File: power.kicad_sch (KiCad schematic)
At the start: 14 parts, among them J3 RAPC722X, J4 Screw_Terminal_01x02, J5 5V, J6 GND, U3 LM2576HVS-5, U4 LM2576HVS-5

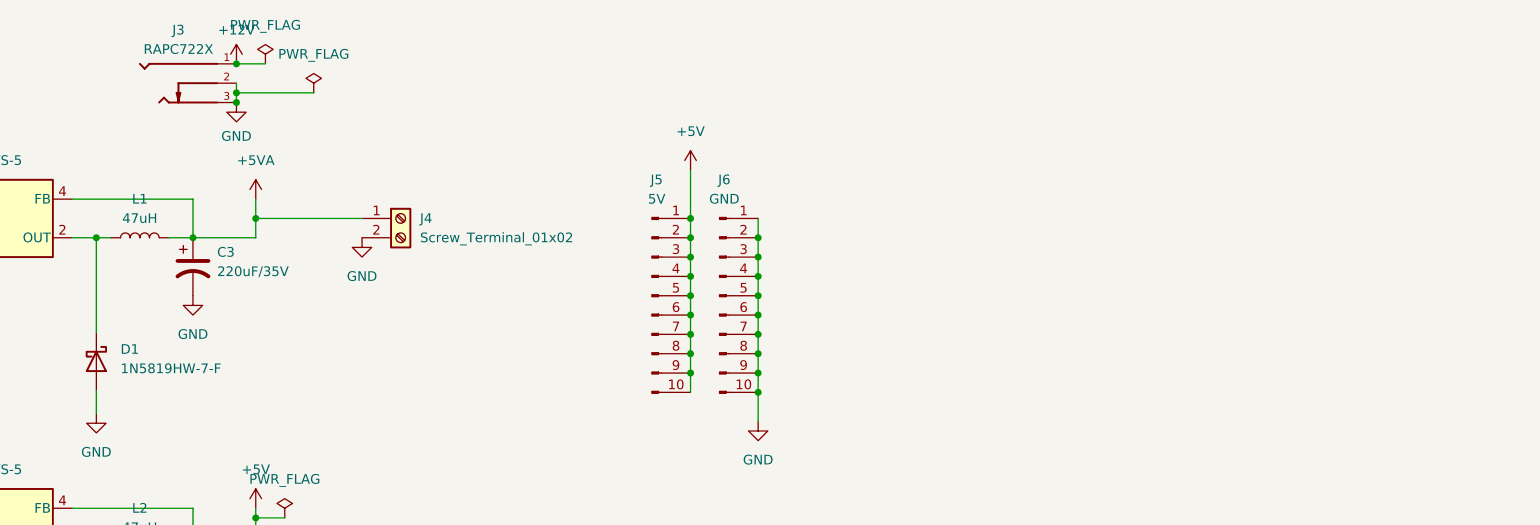
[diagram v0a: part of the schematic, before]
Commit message: Added motor driver
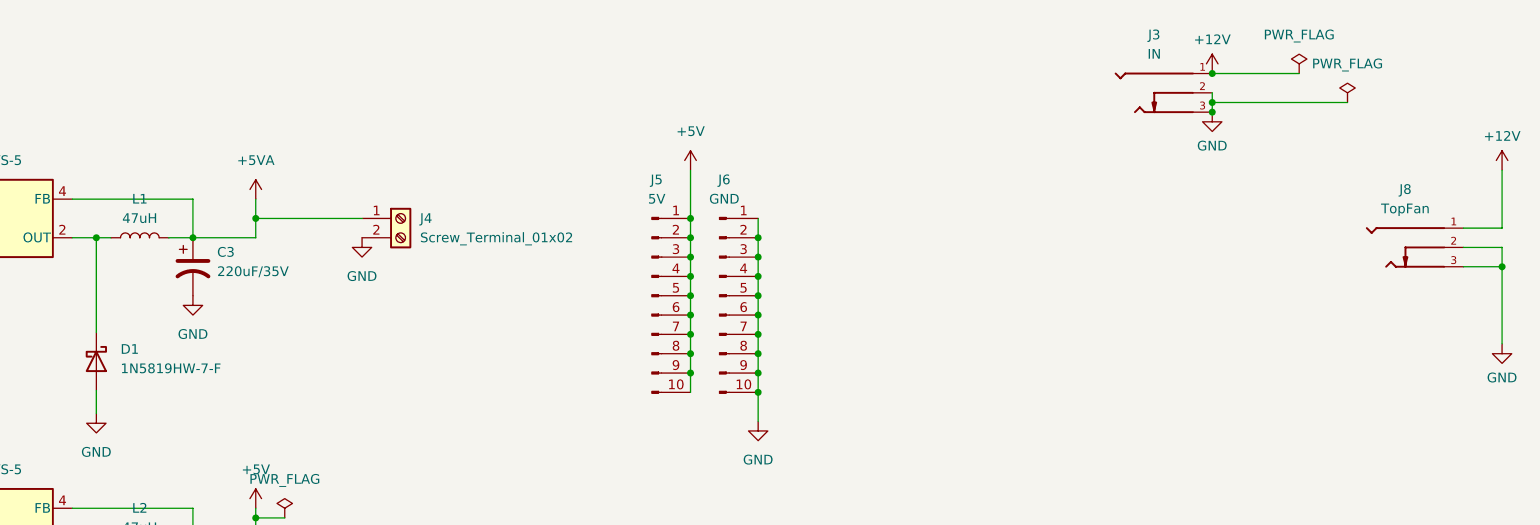
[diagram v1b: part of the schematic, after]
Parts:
- added J8: TopFan, Downloaded_footprints:SWITCHCRAFT_RAPC722X, symbol RAPC722X:RAPC722X
- J3: value RAPC722X -> IN
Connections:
- net +12V: now also J8.1
- net GND: now also J8.2, J8.3
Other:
- moved on the sheet: J3

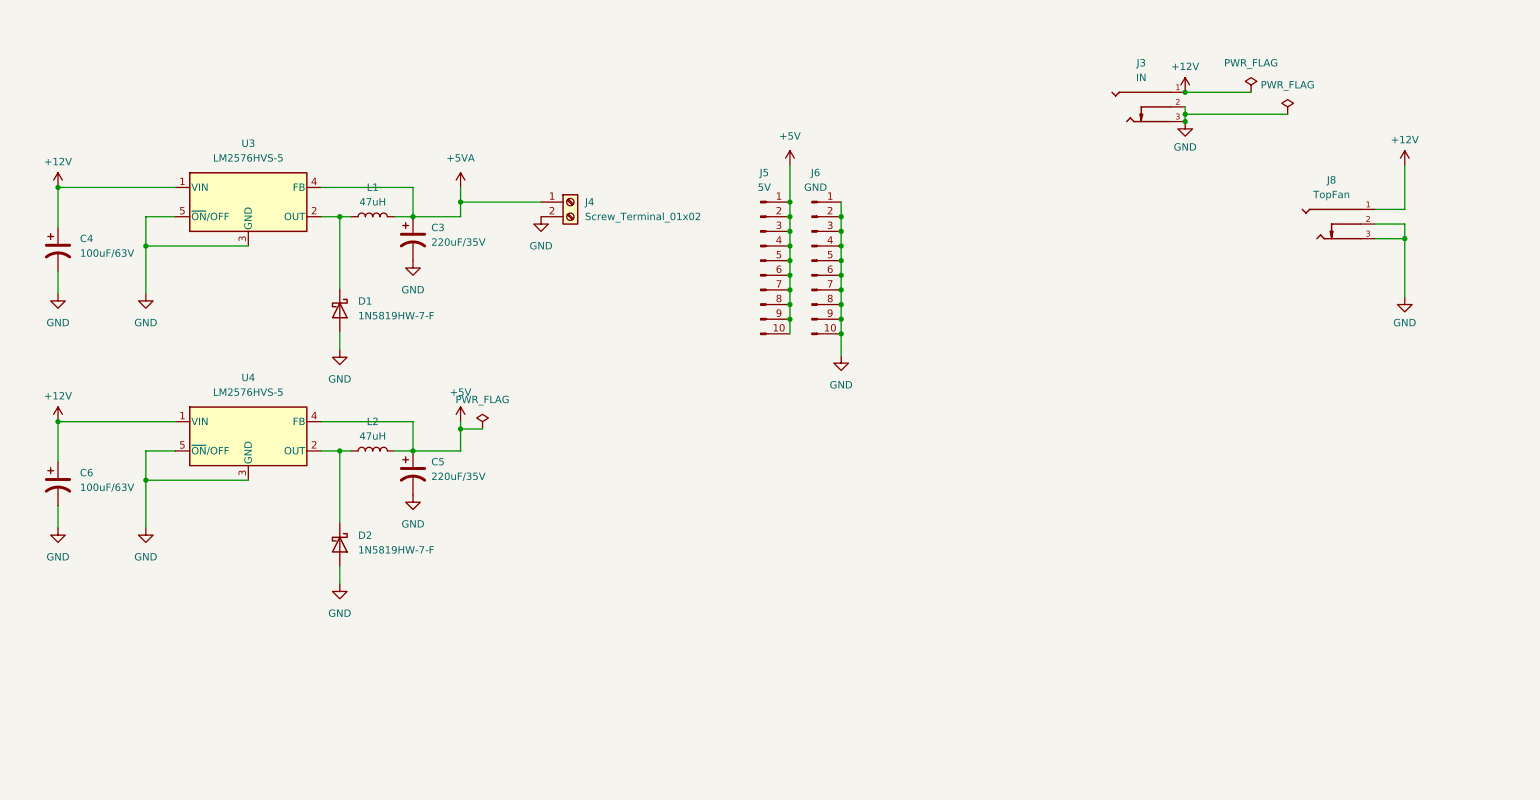
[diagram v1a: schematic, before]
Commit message: power board changes
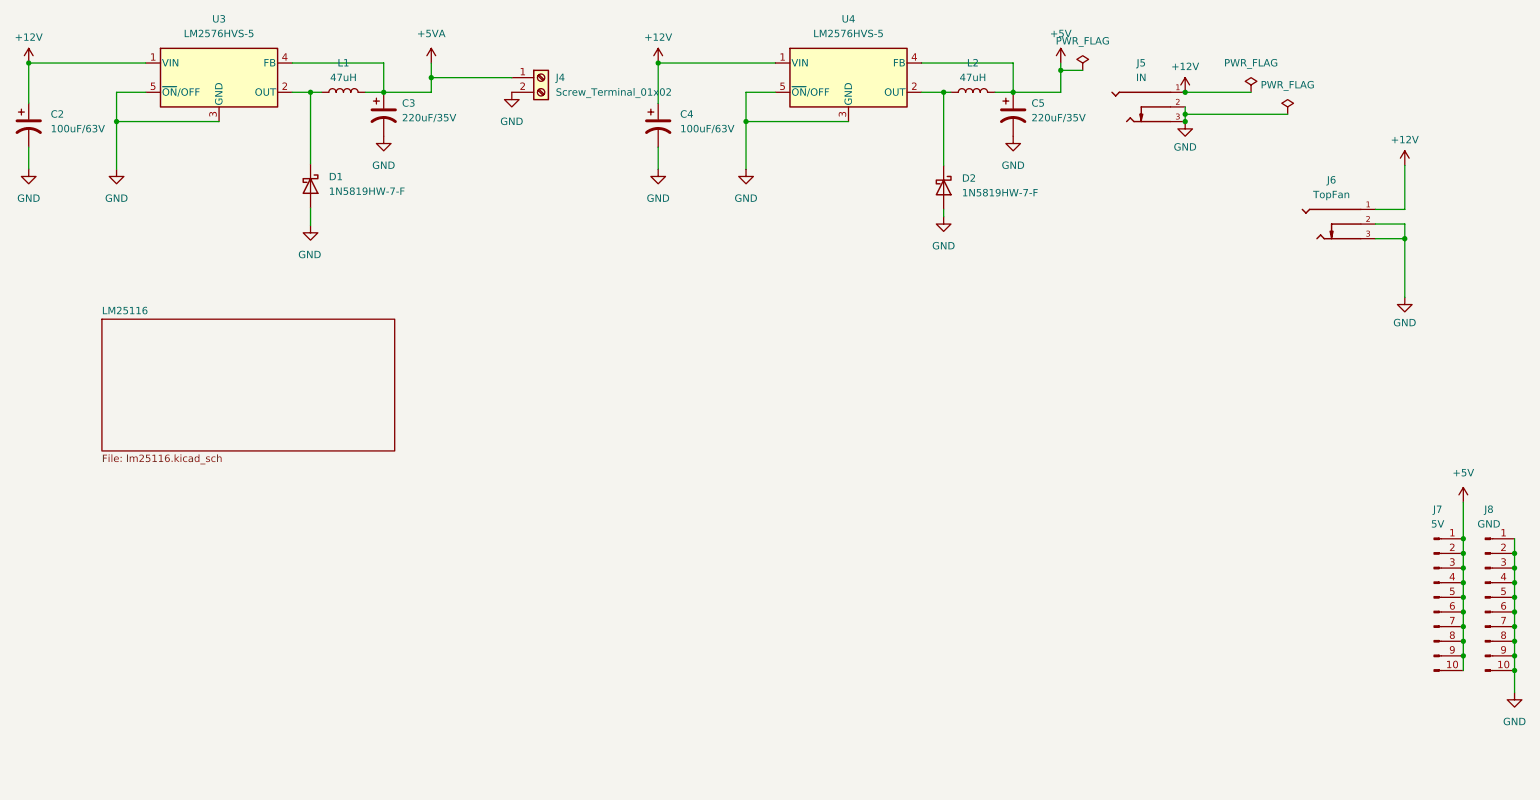
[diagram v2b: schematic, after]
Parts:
- renumbered C4 to C2, C6 to C4, J3 to J5, J8 to J6, J5 to J7, J6 to J8
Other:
- added sheet LM25116 (lm25116.kicad_sch)
- moved on the sheet: C2, C3, C4, C5, D1, D2, J4, J7, J8, L1, L2, U3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

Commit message: New board test
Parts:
- added J9: IN, RAPC722X:SWITCHCRAFT_RAPC722X, symbol RAPC722X:RAPC722X
- J7: renamed from J5; footprint Downloaded_footprints:SWITCHCRAFT_RAPC722X -> RAPC722X:SWITCHCRAFT_RAPC722X
- J8: renamed from J6; footprint Downloaded_footprints:SWITCHCRAFT_RAPC722X -> RAPC722X:SWITCHCRAFT_RAPC722X
- renumbered J7 to J5, J8 to J6
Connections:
- net +5V: now also J9.1
- net GND: now also J9.2, J9.3
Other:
- moved on the sheet: J5, J6

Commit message: Layout changes
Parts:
- removed J7, J9: IN, RAPC722X:SWITCHCRAFT_RAPC722X, symbol RAPC722X:RAPC722X
- removed J8: TopFan, RAPC722X:SWITCHCRAFT_RAPC722X, symbol RAPC722X:RAPC722X
- added J3: 705530002, CONN3_53-0002_MOL, symbol MolexConn:705530002
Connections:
- net +12V: now also J3.3
- net +5V: now also J3.2
- net GND: now also J3.1

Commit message: Updated board
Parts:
- removed C2, C4: 100uF/63V, Capacitor_SMD:CP_Elec_10x10, symbol Device:C_Polarized_US
- removed C3, C5: 220uF/35V, Capacitor_SMD:CP_Elec_10x10, symbol Device:C_Polarized_US
- removed D1, D2: 1N5819HW-7-F, Diode_SMD:D_SOD-123, symbol Device:D_Schottky
- removed J4: Screw_Terminal_01x02, TerminalBlock_MetzConnect:TerminalBlock_MetzConnect_Type011_RT05502HBWC_1x02_P5.00mm_Horizontal, symbol Connector:Screw_Terminal_01x02
- removed L1, L2: 47uH, Inductor_SMD:L_12x12mm_H8mm, symbol Device:L
- removed U3, U4: LM2576HVS-5, Package_TO_SOT_SMD:TO-263-5_TabPin3, symbol Regulator_Switching:LM2576HVS-5
- J3: footprint CONN3_53-0002_MOL -> 705530002:CONN3_53-0002_MOL; LCSC (none) -> C505296; Part Number (none) -> 705530002
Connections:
- net +5V: now also J3.1; no longer J3.2
- net GND: now also J3.2; no longer J3.1
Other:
- removed sheet LM25116
